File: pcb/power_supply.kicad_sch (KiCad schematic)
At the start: 19 parts, among them U1 AMS1117-3.3, U2 ADP2303ARDZ-5.0

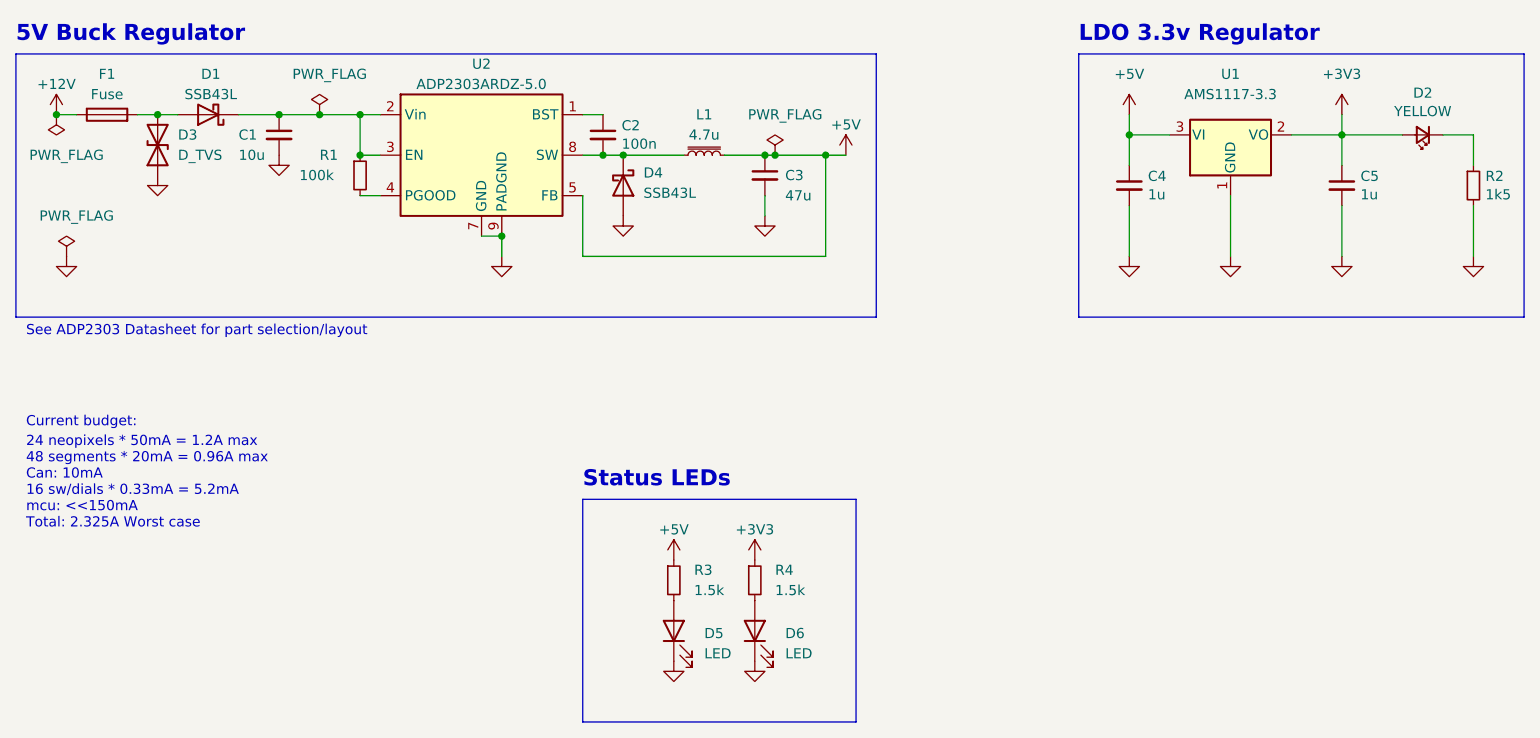
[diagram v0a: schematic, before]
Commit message: Laid out and routed PCB
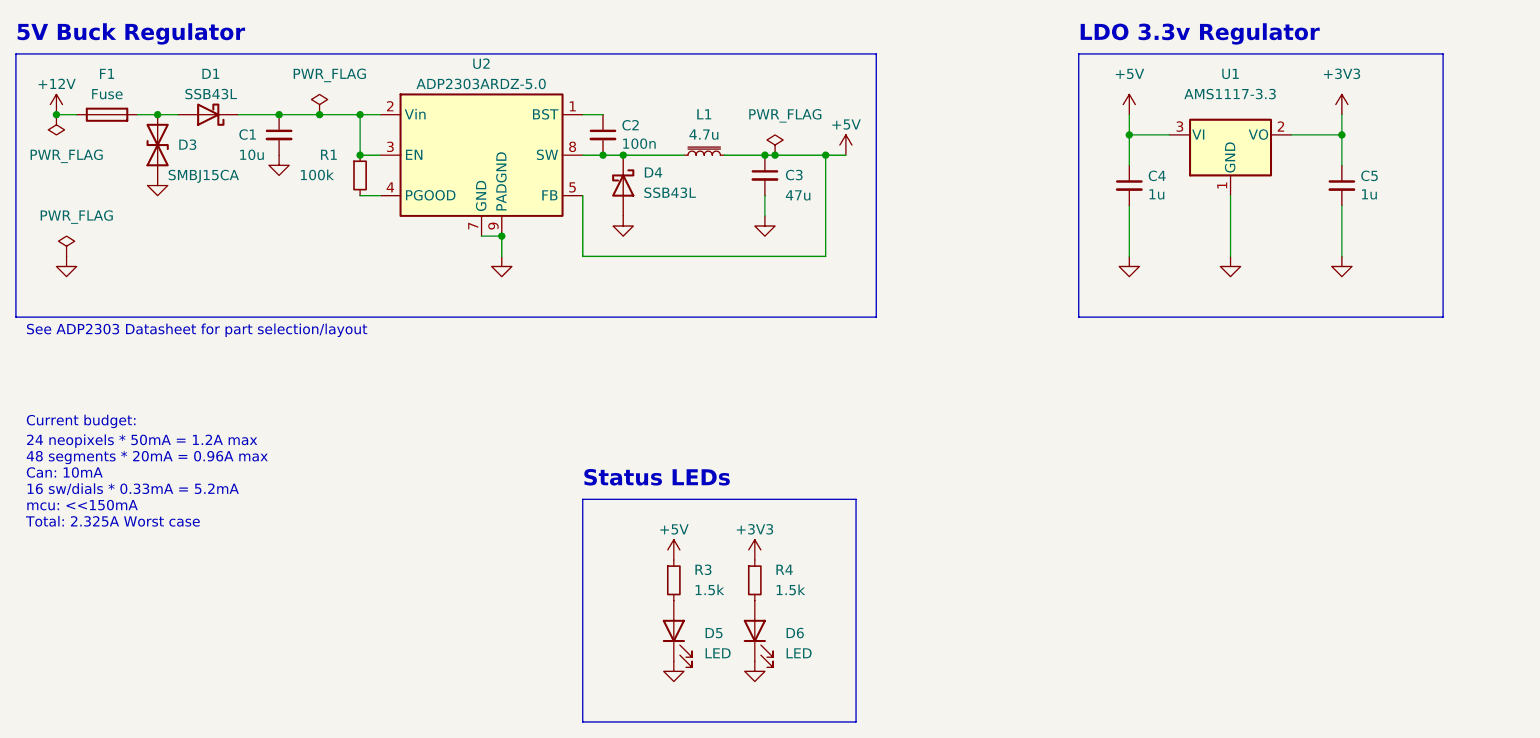
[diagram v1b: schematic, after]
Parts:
- removed D2: YELLOW, LED_SMD:LED_0603_1608Metric, symbol Device:LED_Small
- removed R2: 1k5, Resistor_SMD:R_0402_1005Metric, symbol Device:R_Small
- C1, C3: footprint (none) -> Capacitor_SMD:C_0805_2012Metric
- D1, D4: footprint (none) -> Diode_SMD:D_SMB
- D3: value D_TVS -> SMBJ15CA; footprint (none) -> Diode_SMD:D_SMB
- D5, D6: footprint (none) -> LED_SMD:LED_0603_1608Metric
- F1: footprint (none) -> Fuse:Fuse_0603_1608Metric
- L1: footprint (none) -> Inductor_SMD:L_12x12mm_H6mm
- R1: footprint (none) -> Resistor_SMD:R_0402_1005Metric
- R3, R4: footprint (none) -> Resistor_SMD:R_0603_1608Metric
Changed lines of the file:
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@@
-    (stroke (width 0) (type default) (color 0 0 0 0))
-  )
-  (wire (pts (xy 232.41 80.01) (xy 232.41 73.66))
     (stroke (width 0) (type default) (color 0 0 0 0))
   )
@@
     (stroke (width 0) (type default) (color 0 0 0 0))
   )
-  (wire (pts (xy 232.41 64.77) (xy 232.41 68.58))
-    (stroke (width 0) (type default) (color 0 0 0 0))
-  )
   (wire (pts (xy 110.49 77.47) (xy 107.95 77.47))
     (stroke (width 0) (type default) (color 0 0 0 0))
@@
     (stroke (width 0) (type default) (color 0 0 0 0))
   )
-  (polyline (pts (xy 182.88 54.61) (xy 238.76 54.61))
+  (polyline (pts (xy 182.88 54.61) (xy 228.6 54.61))
     (stroke (width 0) (type default) (color 0 0 0 0))
   )
@@
     (stroke (width 0) (type default) (color 0 0 0 0))
   )
-  (polyline (pts (xy 238.76 87.63) (xy 238.76 54.61))
+  (polyline (pts (xy 228.6 87.63) (xy 228.6 54.61))
     (stroke (width 0) (type default) (color 0 0 0 0))
   )
@@
     (stroke (width 0) (type default) (color 0 0 0 0))
   )
-  (polyline (pts (xy 182.88 87.63) (xy 238.76 87.63))
+  (polyline (pts (xy 182.88 87.63) (xy 228.6 87.63))
     (stroke (width 0) (type default) (color 0 0 0 0))
   )
@@
     (stroke (width 0) (type default) (color 0 0 0 0))
   )
-  (wire (pts (xy 232.41 64.77) (xy 228.6 64.77))
-    (stroke (width 0) (type default) (color 0 0 0 0))
-  )
   (wire (pts (xy 143.51 67.31) (xy 144.78 67.31))
     (stroke (width 0) (type default) (color 0 0 0 0))
@@
   )
   (wire (pts (xy 123.19 67.31) (xy 125.73 67.31))
-    (stroke (width 0) (type default) (color 0 0 0 0))
-  )
-  (wire (pts (xy 223.52 64.77) (xy 215.9 64.77))
     (stroke (width 0) (type default) (color 0 0 0 0))
   )
@@
     (property "Reference" "F1" (id 0) (at 60.96 57.15 90))
     (property "Value" "Fuse" (id 1) (at 60.96 59.69 90))
-    (property "Footprint" "" (id 2) (at 60.96 64.008 90)
+    (property "Footprint" "Fuse:Fuse_0603_1608Metric" (id 2) (at 60.96 64.008 90)
       (effects (font (size 1.27 1.27)) hide)
     )
@@
       (effects (font (size 1.27 1.27)) (justify right))
     )
-    (property "Footprint" "" (id 2) (at 143.51 69.85 0)
+    (property "Footprint" "Capacitor_SMD:C_0805_2012Metric" (id 2) (at 143.51 69.85 0)
       (effects (font (size 1.27 1.27)) hide)
     )
@@
     (pin "1")
     (pin "2")
-  )
-  (symbol (lib_id "power:GND") (at 232.41 80.01 0) (mirror y) (unit 1)
-    (in_bom yes) (on_board yes)
-    (property "Reference" "#PWR013" (id 0) (at 232.41 86.36 0)
-      (effects (font (size 1.27 1.27)) hide)
-    )
-    (property "Value" "GND" (id 1) (at 232.41 83.82 0)
-      (effects (font (size 1.27 1.27)) hide)
-    )
-    (property "Footprint" "" (id 2) (at 232.41 80.01 0)
-      (effects (font (size 1.27 1.27)) hide)
-    )
-    (property "Datasheet" "" (id 3) (at 232.41 80.01 0)
-      (effects (font (size 1.27 1.27)) hide)
-    )
-    (pin "1")
   )
   (symbol (lib_id "power:GND") (at 132.08 130.81 0) (mirror y) (unit 1)
@@
     (property "Reference" "D1" (id 0) (at 73.9775 57.15 0))
     (property "Value" "SSB43L" (id 1) (at 73.9775 59.69 0))
-    (property "Footprint" "" (id 2) (at 73.66 62.23 0)
+    (property "Footprint" "Diode_SMD:D_SMB" (id 2) (at 73.66 62.23 0)
       (effects (font (size 1.27 1.27)) hide)
     )
@@
       (effects (font (size 1.27 1.27)) (justify right))
     )
-    (property "Footprint" "" (id 2) (at 82.55 64.77 0)
+    (property "Footprint" "Capacitor_SMD:C_0805_2012Metric" (id 2) (at 82.55 64.77 0)
       (effects (font (size 1.27 1.27)) hide)
     )
@@
       (effects (font (size 1.27 1.27)) (justify left))
     )
-    (property "Footprint" "" (id 2) (at 132.08 120.65 0)
+    (property "Footprint" "Resistor_SMD:R_0603_1608Metric" (id 2) (at 132.08 120.65 0)
       (effects (font (size 1.27 1.27)) hide)
     )
@@
       (effects (font (size 1.27 1.27)) (justify left))
     )
-    (property "Footprint" "" (id 2) (at 92.71 69.85 0)
+    (property "Footprint" "Resistor_SMD:R_0402_1005Metric" (id 2) (at 92.71 69.85 0)
       (effects (font (size 1.27 1.27)) hide)
     )
@@
       (effects (font (size 1.27 1.27)) (justify left))
     )
-    (property "Footprint" "" (id 2) (at 142.24 120.65 0)
+    (property "Footprint" "Resistor_SMD:R_0603_1608Metric" (id 2) (at 142.24 120.65 0)
       (effects (font (size 1.27 1.27)) hide)
     )
@@
     (property "Reference" "L1" (id 0) (at 135.89 62.23 90))
     (property "Value" "4.7u" (id 1) (at 135.89 64.77 90))
-    (property "Footprint" "" (id 2) (at 135.89 67.31 0)
+    (property "Footprint" "Inductor_SMD:L_12x12mm_H6mm" (id 2) (at 135.89 67.31 0)
       (effects (font (size 1.27 1.27)) hide)
     )
@@
       (effects (font (size 1.27 1.27)) (justify right))
     )
-    (property "Footprint" "" (id 2) (at 132.08 127 0)
+    (property "Footprint" "LED_SMD:LED_0603_1608Metric" (id 2) (at 132.08 127 0)
       (effects (font (size 1.27 1.27)) hide)
     )
@@
     (pin "9")
   )
-  (symbol (lib_id "Device:R_Small") (at 232.41 71.12 0) (unit 1)
-    (in_bom yes) (on_board yes)
-    (property "Reference" "R2" (id 0) (at 233.9086 69.9516 0)
-      (effects (font (size 1.27 1.27)) (justify left))
-    )
-    (property "Value" "1k5" (id 1) (at 233.9086 72.263 0)
-      (effects (font (size 1.27 1.27)) (justify left))
-    )
-    (property "Footprint" "Resistor_SMD:R_0402_1005Metric" (id 2) (at 232.41 71.12 0)
-      (effects (font (size 1.27 1.27)) hide)
-    )
-    (property "Datasheet" "~" (id 3) (at 232.41 71.12 0)
-      (effects (font (size 1.27 1.27)) hide)
-    )
-    (property "LCSC" "C25867" (id 5) (at 232.41 71.12 0)
-      (effects (font (size 1.27 1.27)) hide)
-    )
-    (pin "1")
-    (pin "2")
-  )
   (symbol (lib_id "Device:D_Schottky") (at 125.73 71.12 270) (unit 1)
     (in_bom yes) (on_board yes) (fields_autoplaced)
@@
       (effects (font (size 1.27 1.27)) (justify left))
     )
-    (property "Footprint" "" (id 2) (at 125.73 71.12 0)
+    (property "Footprint" "Diode_SMD:D_SMB" (id 2) (at 125.73 71.12 0)
       (effects (font (size 1.27 1.27)) hide)
     )
@@
     (pin "1")
   )
-  (symbol (lib_id "Device:LED_Small") (at 226.06 64.77 180) (unit 1)
-    (in_bom yes) (on_board yes)
-    (property "Reference" "D2" (id 0) (at 226.06 59.5122 0))
-    (property "Value" "YELLOW" (id 1) (at 226.06 61.8236 0))
-    (property "Footprint" "LED_SMD:LED_0603_1608Metric" (id 2) (at 226.06 64.77 90)
-      (effects (font (size 1.27 1.27)) hide)
-    )
-    (property "Datasheet" "~" (id 3) (at 226.06 64.77 90)
-      (effects (font (size 1.27 1.27)) hide)
-    )
-    (property "LCSC" "C72038" (id 5) (at 226.06 64.77 0)
-      (effects (font (size 1.27 1.27)) hide)
-    )
-    (pin "1")
-    (pin "2")
-  )
   (symbol (lib_id "Device:D_TVS") (at 67.31 66.04 90) (unit 1)
-    (in_bom yes) (on_board yes) (fields_autoplaced)
-    (property "Reference" "D3" (id 0) (at 69.85 64.7699 90)
-      (effects (font (size 1.27 1.27)) (justify right))
-    )
-    (property "Value" "D_TVS" (id 1) (at 69.85 67.3099 90)
-      (effects (font (size 1.27 1.27)) (justify right))
-    )
-    (property "Footprint" "" (id 2) (at 67.31 66.04 0)
+    (in_bom yes) (on_board yes)
+    (property "Reference" "D3" (id 0) (at 69.85 66.04 90)
+      (effects (font (size 1.27 1.27)) (justify right))
+    )
+    (property "Value" "SMBJ15CA" (id 1) (at 68.58 69.85 90)
+      (effects (font (size 1.27 1.27)) (justify right))
+    )
+    (property "Footprint" "Diode_SMD:D_SMB" (id 2) (at 67.31 66.04 0)
       (effects (font (size 1.27 1.27)) hide)
     )
@@
       (effects (font (size 1.27 1.27)) (justify right))
     )
-    (property "Footprint" "" (id 2) (at 142.24 127 0)
-      (effects (font (size 1.27 1.27)) hide)
-    )
+    (property "Footprint" "LED_SMD:LED_0603_1608Metric" (id 2) (at 142.24 127 0)
+      (effects (font (size 1.27 1.27)) hide)
+    )
